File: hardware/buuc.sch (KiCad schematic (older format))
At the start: 27 parts, among them P1 USB_OTG, P2 CONN_01X02, Q1 NDS8434, U1 BOOST_REGULATOR, U2 MCP73842-840I/UN, U3 MIC2005A

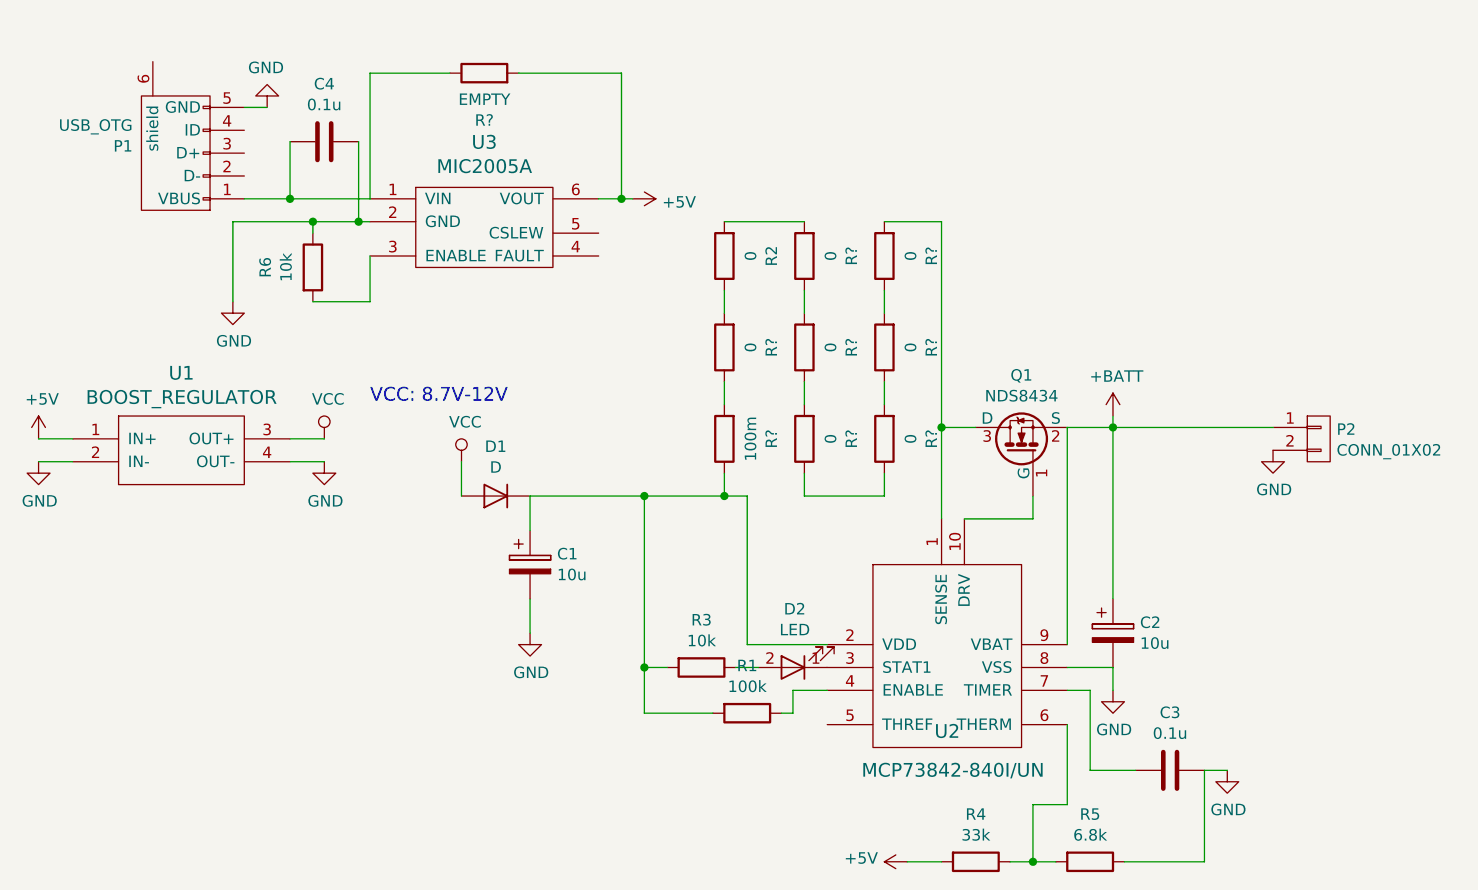
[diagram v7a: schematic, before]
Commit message: Switch to through-hole USB adapter; the SMD component is a little too jiggly, and I don't have better ones on-hand at the moment.
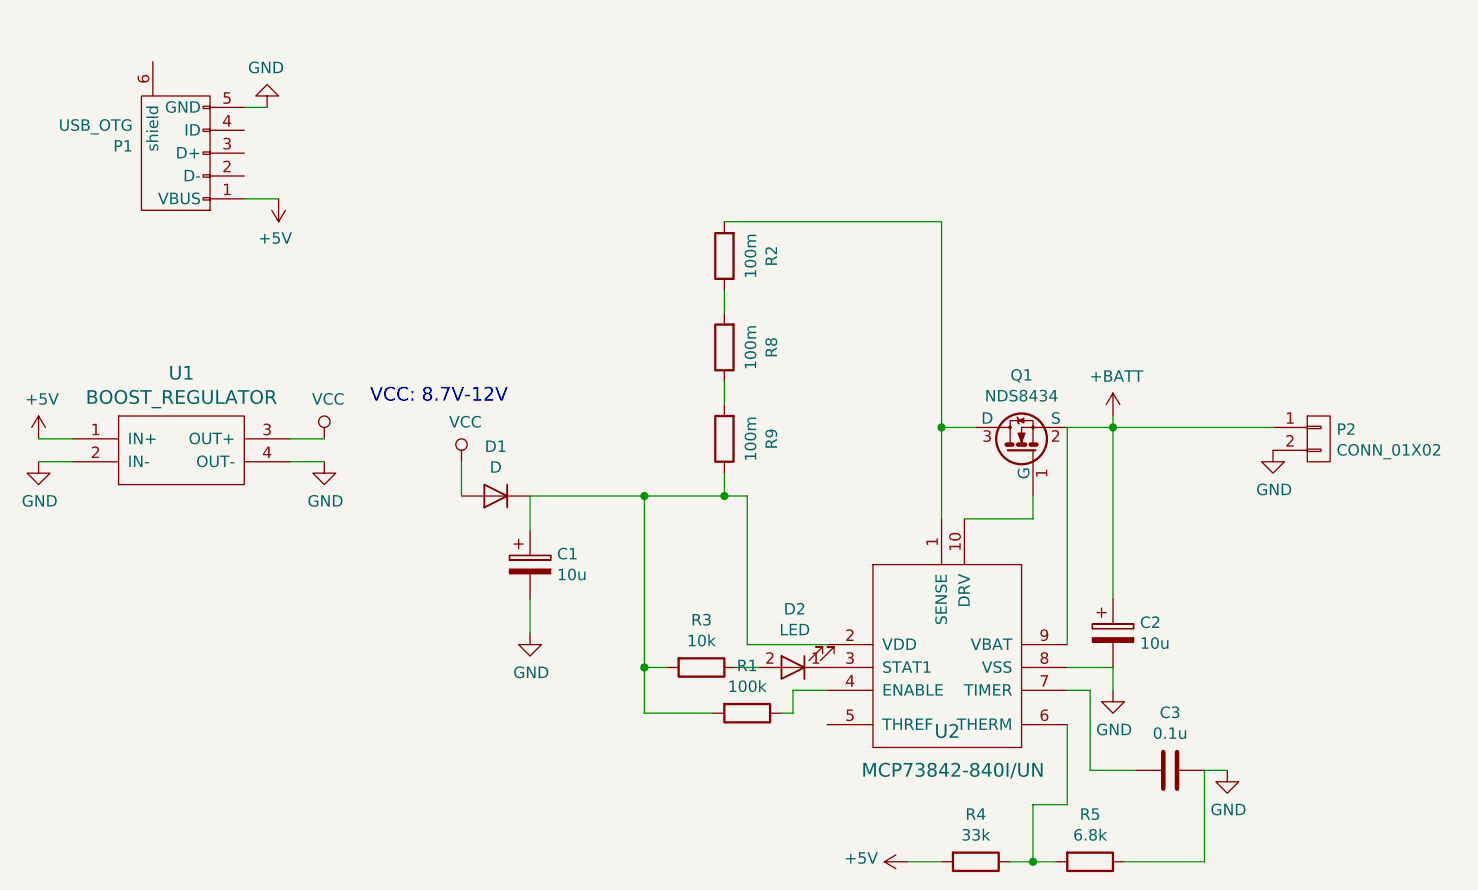
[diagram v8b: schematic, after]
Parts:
- removed C4: 0.1u, coddingtonbear/coddingtonbear.pretty:0805_Milling, symbol C
- removed R6: 10k, coddingtonbear/coddingtonbear.pretty:0805_Milling, symbol R
- removed R? (x6): 0, coddingtonbear/coddingtonbear.pretty:0805_Milling, symbol R
- removed R?: EMPTY, coddingtonbear/coddingtonbear.pretty:0805_Milling, symbol R
- removed U3: MIC2005A, adamgreig/agg-kicad/agg.pretty:SOT-23-6, symbol MIC2005A-RESCUE-buuc
- P1: footprint coddingtonbear/coddingtonbear.pretty:MICRO-B_USB-INVERTED -> coddingtonbear/coddingtonbear.pretty:USB_Thru_hole
- R2: value 0 -> 100m
- R8: renamed from R?; value 0 -> 100m
- gave numbers to parts that had none: 1
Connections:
- net +5V: now also P1.1 (VBUS)
- net at Q1.3 (D), U2.1 (SENSE): now also R2.2
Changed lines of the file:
@@
 LIBS:contrib
 LIBS:valves
+LIBS:coddingtonbear
 LIBS:buuc-cache
 EELAYER 26 0
@@
 F 0 "P1" V 1580 1638 50  0000 L CNN
 F 1 "USB_OTG" V 1671 1638 50  0000 L CNN
-F 2 "coddingtonbear/coddingtonbear.pretty:MICRO-B_USB-INVERTED" V 1500 1350 50  0001 C CNN
+F 2 "coddingtonbear/coddingtonbear.pretty:USB_Thru_hole" V 1500 1350 50  0001 C CNN
 F 3 "" V 1500 1350 50  0000 C CNN
 	1    1550 1450
@@
 $Comp
 L +5V #PWR01
-U 1 1 59AF62AD
-P 3550 1650
-F 0 "#PWR01" H 3550 1500 50  0001 C CNN
-F 1 "+5V" V 3565 1778 50  0000 L CNN
-F 2 "" H 3550 1650 50  0000 C CNN
-F 3 "" H 3550 1650 50  0000 C CNN
-	1    3550 1650
-	0    1    1    0
-$EndComp
-$Comp
-L +5V #PWR02
 U 1 1 59AF62D9
 P 950 2700
-F 0 "#PWR02" H 950 2550 50  0001 C CNN
+F 0 "#PWR01" H 950 2550 50  0001 C CNN
 F 1 "+5V" H 965 2873 50  0000 C CNN
 F 2 "" H 950 2700 50  0000 C CNN
@@
 $EndComp
 $Comp
-L GND #PWR03
+L GND #PWR02
 U 1 1 59AF6327
 P 950 2800
-F 0 "#PWR03" H 950 2550 50  0001 C CNN
+F 0 "#PWR02" H 950 2550 50  0001 C CNN
 F 1 "GND" H 955 2627 50  0000 C CNN
 F 2 "" H 950 2800 50  0000 C CNN
@@
 $EndComp
 $Comp
-L GND #PWR04
+L GND #PWR03
 U 1 1 59AF634E
 P 2200 2800
-F 0 "#PWR04" H 2200 2550 50  0001 C CNN
+F 0 "#PWR03" H 2200 2550 50  0001 C CNN
 F 1 "GND" H 2205 2627 50  0000 C CNN
 F 2 "" H 2200 2800 50  0000 C CNN
@@
 $EndComp
 $Comp
-L GND #PWR05
+L GND #PWR04
 U 1 1 59AF6362
 P 1950 1250
-F 0 "#PWR05" H 1950 1000 50  0001 C CNN
+F 0 "#PWR04" H 1950 1000 50  0001 C CNN
 F 1 "GND" H 1955 1077 50  0000 C CNN
 F 2 "" H 1950 1250 50  0000 C CNN
@@
 $EndComp
 Wire Wire Line
-	1850 1650 2400 1650
-Wire Wire Line
 	1950 1250 1850 1250
 Wire Wire Line
@@
 	950  2700 1100 2700
 $Comp
-L VCC #PWR06
+L VCC #PWR05
 U 1 1 59AF63A7
 P 2200 2700
-F 0 "#PWR06" H 2200 2550 50  0001 C CNN
+F 0 "#PWR05" H 2200 2550 50  0001 C CNN
 F 1 "VCC" H 2217 2873 50  0000 C CNN
 F 2 "" H 2200 2700 50  0000 C CNN
@@
 	2050 2700 2200 2700
 $Comp
-L VCC #PWR07
+L VCC #PWR06
 U 1 1 59AF6811
 P 2800 2800
-F 0 "#PWR07" H 2800 2650 50  0001 C CNN
+F 0 "#PWR06" H 2800 2650 50  0001 C CNN
 F 1 "VCC" H 2817 2973 50  0000 C CNN
 F 2 "" H 2800 2800 50  0000 C CNN
@@
 $EndComp
 $Comp
-L GND #PWR08
+L GND #PWR07
 U 1 1 59AF6994
 P 3100 3550
-F 0 "#PWR08" H 3100 3300 50  0001 C CNN
+F 0 "#PWR07" H 3100 3300 50  0001 C CNN
 F 1 "GND" H 3105 3377 50  0000 C CNN
 F 2 "" H 3100 3550 50  0000 C CNN
@@
 P 3950 1900
 F 0 "R2" V 3743 1900 50  0000 C CNN
-F 1 "0" V 3834 1900 50  0000 C CNN
+F 1 "100m" V 3834 1900 50  0000 C CNN
 F 2 "coddingtonbear/coddingtonbear.pretty:0805_Milling" V 3880 1900 50  0001 C CNN
 F 3 "" H 3950 1900 50  0000 C CNN
@@
 	5650 3700 5450 3700
 $Comp
-L GND #PWR09
+L GND #PWR08
 U 1 1 59AF75B2
 P 5650 3800
-F 0 "#PWR09" H 5650 3550 50  0001 C CNN
+F 0 "#PWR08" H 5650 3550 50  0001 C CNN
 F 1 "GND" H 5655 3627 50  0000 C CNN
 F 2 "" H 5650 3800 50  0000 C CNN
@@
 Connection ~ 5650 2650
 $Comp
-L +BATT #PWR010
+L +BATT #PWR09
 U 1 1 59AF7B81
 P 5650 2600
-F 0 "#PWR010" H 5650 2450 50  0001 C CNN
+F 0 "#PWR09" H 5650 2450 50  0001 C CNN
 F 1 "+BATT" H 5665 2773 50  0000 C CNN
 F 2 "" H 5650 2600 50  0000 C CNN
@@
 $EndComp
 $Comp
-L GND #PWR011
+L GND #PWR010
 U 1 1 59AF7BB9
 P 6350 2750
-F 0 "#PWR011" H 6350 2500 50  0001 C CNN
+F 0 "#PWR010" H 6350 2500 50  0001 C CNN
 F 1 "GND" H 6355 2577 50  0000 C CNN
 F 2 "" H 6350 2750 50  0000 C CNN
@@
 $EndComp
 $Comp
-L GND #PWR012
+L GND #PWR011
 U 1 1 59AFAA9C
 P 6150 4150
-F 0 "#PWR012" H 6150 3900 50  0001 C CNN
+F 0 "#PWR011" H 6150 3900 50  0001 C CNN
 F 1 "GND" H 6155 3977 50  0000 C CNN
 F 2 "" H 6150 4150 50  0000 C CNN
@@
 Connection ~ 5300 4550
 $Comp
-L +5V #PWR013
+L +5V #PWR012
 U 1 1 59AFAFDA
 P 4750 4550
-F 0 "#PWR013" H 4750 4400 50  0001 C CNN
+F 0 "#PWR012" H 4750 4400 50  0001 C CNN
 F 1 "+5V" V 4765 4678 50  0000 L CNN
 F 2 "" H 4750 4550 50  0000 C CNN
@@
 	4750 4550 4900 4550
 $Comp
-L MIC2005A-RESCUE-buuc U3
-U 1 1 59BADA49
-P 2900 1750
-F 0 "U3" H 2900 2097 60  0000 C CNN
-F 1 "MIC2005A" H 2900 1991 60  0000 C CNN
-F 2 "adamgreig/agg-kicad/agg.pretty:SOT-23-6" H 2900 1750 60  0001 C CNN
-F 3 "" H 2900 1750 60  0001 C CNN
-	1    2900 1750
-	1    0    0    -1
-$EndComp
-Wire Wire Line
-	3550 1650 3400 1650
-$Comp
-L GND #PWR014
-U 1 1 59BADB64
-P 1800 2100
-F 0 "#PWR014" H 1800 1850 50  0001 C CNN
-F 1 "GND" H 1805 1927 50  0000 C CNN
-F 2 "" H 1800 2100 50  0000 C CNN
-F 3 "" H 1800 2100 50  0000 C CNN
-	1    1800 2100
-	1    0    0    -1
-$EndComp
-Wire Wire Line
-	1800 1750 2400 1750
-$Comp
-L R R6
-U 1 1 59BADC60
-P 2150 1950
-F 0 "R6" V 1943 1950 50  0000 C CNN
-F 1 "10k" V 2034 1950 50  0000 C CNN
-F 2 "coddingtonbear/coddingtonbear.pretty:0805_Milling" V 2080 1950 50  0001 C CNN
-F 3 "" H 2150 1950 50  0000 C CNN
-	1    2150 1950
-	1    0    0    -1
-$EndComp
-$Comp
-L C C4
-U 1 1 59BAE16D
-P 2200 1400
-F 0 "C4" V 1948 1400 50  0000 C CNN
-F 1 "0.1u" V 2039 1400 50  0000 C CNN
-F 2 "coddingtonbear/coddingtonbear.pretty:0805_Milling" H 2238 1250 50  0001 C CNN
-F 3 "" H 2200 1400 50  0000 C CNN
-	1    2200 1400
-	0    1    1    0
-$EndComp
-Wire Wire Line
-	2350 1400 2350 1750
-Connection ~ 2350 1750
-Wire Wire Line
-	2050 1400 2050 1650
-Connection ~ 2050 1650
-Wire Wire Line
-	2150 1800 2150 1750
-Connection ~ 2150 1750
-Wire Wire Line
-	2150 2100 2400 2100
-Wire Wire Line
-	2400 2100 2400 1900
-Wire Wire Line
-	1800 1750 1800 2100
-$Comp
-L R R?
+L R R9
 U 1 1 59C097A1
 P 3950 2700
-F 0 "R?" V 3743 2700 50  0000 C CNN
+F 0 "R9" V 3743 2700 50  0000 C CNN
 F 1 "100m" V 3834 2700 50  0000 C CNN
 F 2 "coddingtonbear/coddingtonbear.pretty:0805_Milling" V 3880 2700 50  0001 C CNN
@@
 $EndComp
 $Comp
-L R R?
+L R R8
 U 1 1 59C0980C
 P 3950 2300
-F 0 "R?" V 3743 2300 50  0000 C CNN
-F 1 "0" V 3834 2300 50  0000 C CNN
+F 0 "R8" V 3743 2300 50  0000 C CNN
+F 1 "100m" V 3834 2300 50  0000 C CNN
 F 2 "coddingtonbear/coddingtonbear.pretty:0805_Milling" V 3880 2300 50  0001 C CNN
 F 3 "" H 3950 2300 50  0000 C CNN
@@
 	-1   0    0    1
 $EndComp
-$Comp
-L R R?
-U 1 1 59C09A2E
-P 4300 2700
-F 0 "R?" V 4093 2700 50  0000 C CNN
-F 1 "0" V 4184 2700 50  0000 C CNN
-F 2 "coddingtonbear/coddingtonbear.pretty:0805_Milling" V 4230 2700 50  0001 C CNN
-F 3 "" H 4300 2700 50  0000 C CNN
-	1    4300 2700
-	-1   0    0    1
-$EndComp
-$Comp
-L R R?
-U 1 1 59C09A8A
-P 4300 2300
-F 0 "R?" V 4093 2300 50  0000 C CNN
-F 1 "0" V 4184 2300 50  0000 C CNN
-F 2 "coddingtonbear/coddingtonbear.pretty:0805_Milling" V 4230 2300 50  0001 C CNN
-F 3 "" H 4300 2300 50  0000 C CNN
-	1    4300 2300
-	-1   0    0    1
-$EndComp
-$Comp
-L R R?
-U 1 1 59C09AD2
-P 4300 1900
-F 0 "R?" V 4093 1900 50  0000 C CNN
-F 1 "0" V 4184 1900 50  0000 C CNN
-F 2 "coddingtonbear/coddingtonbear.pretty:0805_Milling" V 4230 1900 50  0001 C CNN
-F 3 "" H 4300 1900 50  0000 C CNN
-	1    4300 1900
-	-1   0    0    1
-$EndComp
-$Comp
-L R R?
-U 1 1 59C09B3C
-P 4650 2700
-F 0 "R?" V 4443 2700 50  0000 C CNN
-F 1 "0" V 4534 2700 50  0000 C CNN
-F 2 "coddingtonbear/coddingtonbear.pretty:0805_Milling" V 4580 2700 50  0001 C CNN
-F 3 "" H 4650 2700 50  0000 C CNN
-	1    4650 2700
-	-1   0    0    1
-$EndComp
-$Comp
-L R R?
-U 1 1 59C0A0C4
-P 4650 2300
-F 0 "R?" V 4443 2300 50  0000 C CNN
-F 1 "0" V 4534 2300 50  0000 C CNN
-F 2 "coddingtonbear/coddingtonbear.pretty:0805_Milling" V 4580 2300 50  0001 C CNN
-F 3 "" H 4650 2300 50  0000 C CNN
-	1    4650 2300
-	-1   0    0    1
-$EndComp
-$Comp
-L R R?
-U 1 1 59C0A112
-P 4650 1900
-F 0 "R?" V 4443 1900 50  0000 C CNN
-F 1 "0" V 4534 1900 50  0000 C CNN
-F 2 "coddingtonbear/coddingtonbear.pretty:0805_Milling" V 4580 1900 50  0001 C CNN
-F 3 "" H 4650 1900 50  0000 C CNN
-	1    4650 1900
-	-1   0    0    1
-$EndComp
 Wire Wire Line
 	4050 2950 3100 2950
@@
 	3950 2150 3950 2050
 Wire Wire Line
-	3950 1750 4300 1750
-Wire Wire Line
-	4300 2050 4300 2150
-Wire Wire Line
-	4300 2450 4300 2550
-Wire Wire Line
-	4300 2850 4300 2950
-Wire Wire Line
-	4300 2950 4650 2950
-Wire Wire Line
-	4650 2950 4650 2850
-Wire Wire Line
-	4650 2550 4650 2450
-Wire Wire Line
-	4650 2150 4650 2050
-Wire Wire Line
-	4650 1750 4900 1750
+	3950 1750 4900 1750
 Connection ~ 4900 2650
 $Comp
-L R R?
-U 1 1 59C0A9C6
-P 2900 1100
-F 0 "R?" V 2693 1100 50  0000 C CNN
-F 1 "EMPTY" V 2784 1100 50  0000 C CNN
-F 2 "coddingtonbear/coddingtonbear.pretty:0805_Milling" V 2830 1100 50  0001 C CNN
-F 3 "" H 2900 1100 50  0000 C CNN
-	1    2900 1100
-	0    -1   -1   0
-$EndComp
-Wire Wire Line
-	2400 1650 2400 1100
-Wire Wire Line
-	2400 1100 2750 1100
-Wire Wire Line
-	3050 1100 3500 1100
-Wire Wire Line
-	3500 1100 3500 1650
-Connection ~ 3500 1650
+L +5V #PWR013
+U 1 1 59C5BF18
+P 2000 1650
+F 0 "#PWR013" H 2000 1500 50  0001 C CNN
+F 1 "+5V" H 2015 1823 50  0000 C CNN
+F 2 "" H 2000 1650 50  0000 C CNN
+F 3 "" H 2000 1650 50  0000 C CNN
+	1    2000 1650
+	-1   0    0    1
+$EndComp
+Wire Wire Line
+	1850 1650 2000 1650
 $EndSCHEMATC
